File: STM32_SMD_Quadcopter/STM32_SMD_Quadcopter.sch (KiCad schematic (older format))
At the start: 70 parts, among them J1 PWR, J2 USB_B_Micro, J3 Micro_SD_Card_Det, J4 DEBUG, J5 DSMX, M1 Brushed_DC, M2 Brushed_DC, M3 Brushed_DC, M4 Brushed_DC, Q1 IRLML6244TR, Q2 IRLML6244TR, Q3 IRLML6244TR, Q4 IRLML6244TR, Q5 2N7002, SW1 SW_Push, U1 AMS1117-3.3, U2 AMS1117-1.8, U3 FT230XQ, U4 STM32F446RETx, U5 ICM-20948, Y1 16MHz X322516MLB4SI

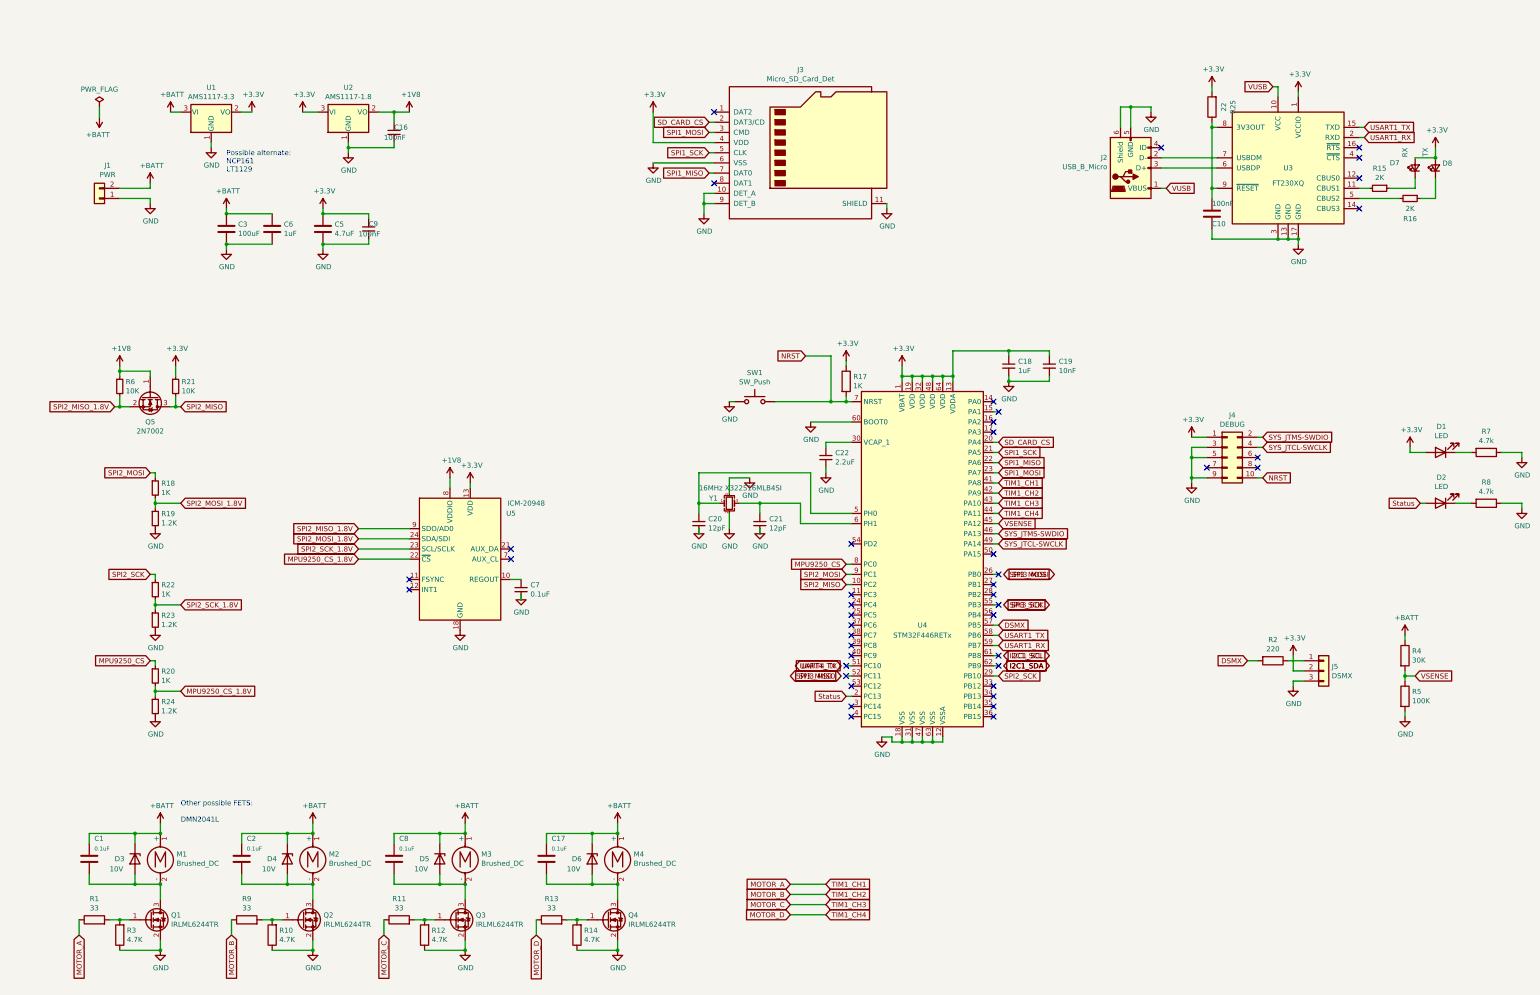
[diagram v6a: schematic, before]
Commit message: completed switchover to MPU6050
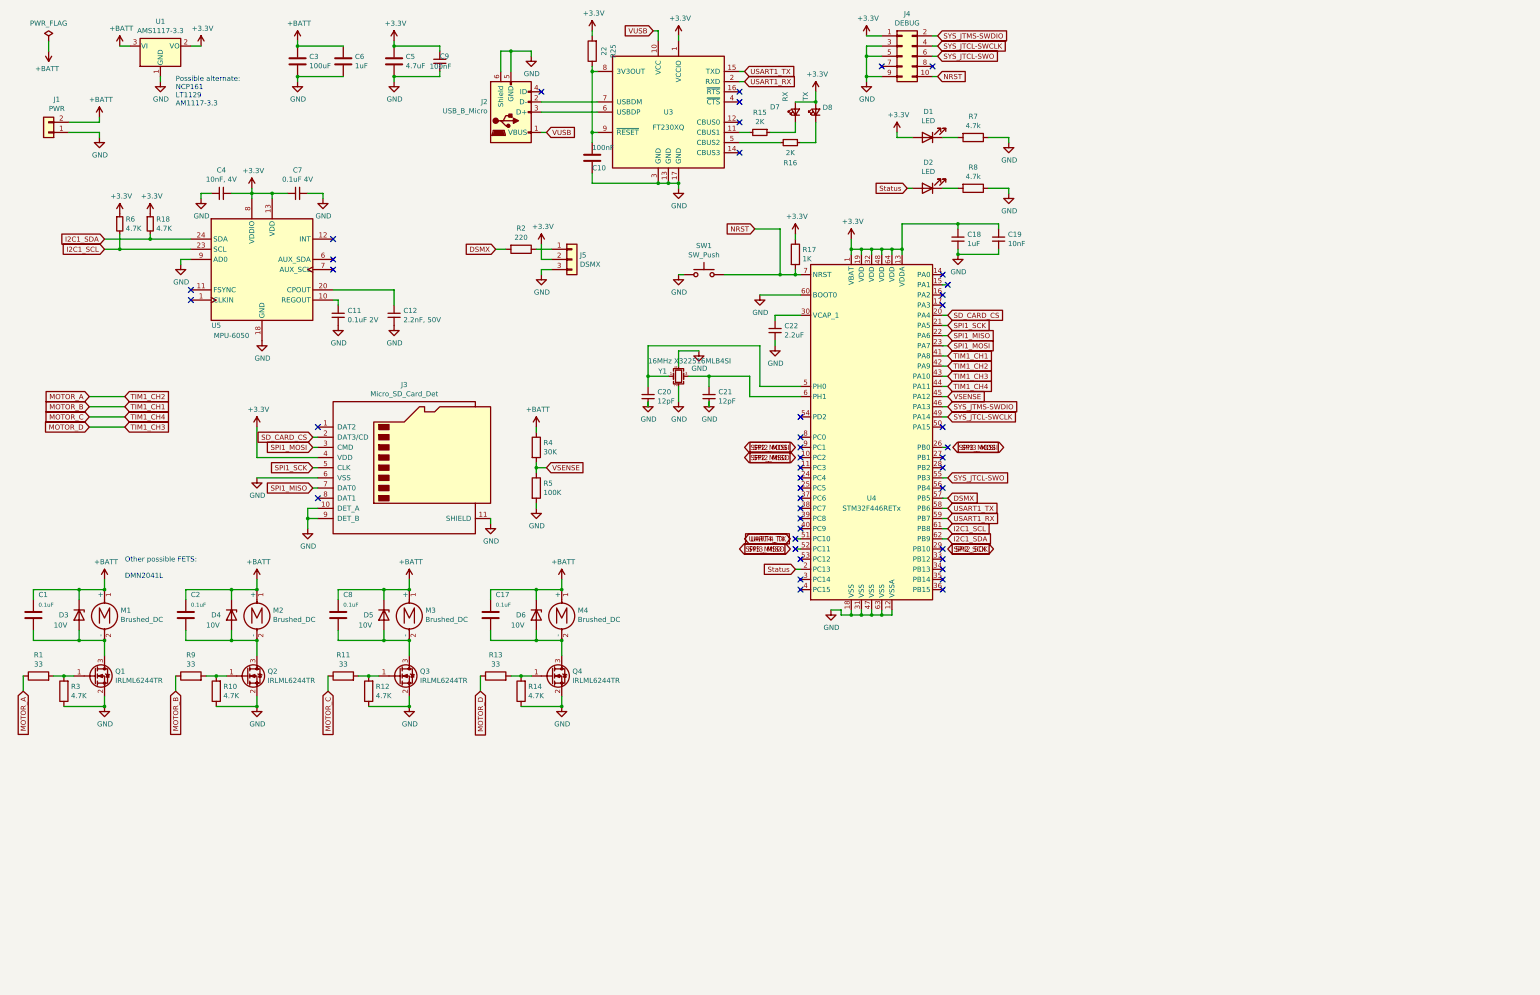
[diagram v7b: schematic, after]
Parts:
- removed C16: 100nF, Capacitor_SMD:C_0402_1005Metric, symbol Device:C_Small
- removed Q5: 2N7002, Package_TO_SOT_SMD:SOT-23, symbol Transistor_FET:2N7002
- removed R19, R23, R24: 1.2K, Resistor_SMD:R_0402_1005Metric, symbol Device:R_Small
- removed R20, R22: 1K, Resistor_SMD:R_0402_1005Metric, symbol Device:R_Small
- removed R21: 10K, Resistor_SMD:R_0402_1005Metric, symbol Device:R_Small
- removed U2: AMS1117-1.8, Package_TO_SOT_SMD:SOT-223-3_TabPin2, symbol Regulator_Linear:AMS1117-1.8
- removed U5: ICM-20948, Sensor_Motion:InvenSense_QFN-24_3x3mm_P0.4mm, symbol Sensor_Motion:ICM-20948
- added C11: 0.1uF 2V, Capacitor_SMD:C_0402_1005Metric, symbol Device:C_Small
- added C12: 2.2nF, 50V, Capacitor_SMD:C_0805_2012Metric, symbol Device:C_Small
- added C4: 10nF, 4V, Capacitor_SMD:C_0402_1005Metric, symbol Device:C_Small
- added U5: MPU-6050, Sensor_Motion:InvenSense_QFN-24_4x4mm_P0.5mm, symbol Sensor_Motion:MPU-6050
- C7: value 0.1uF -> 0.1uF 4V
- R18: value 1K -> 4.7K; footprint Resistor_SMD:R_0402_1005Metric -> Resistor_SMD:R_0603_1608Metric
- R6: value 10K -> 4.7K; footprint Resistor_SMD:R_0402_1005Metric -> Resistor_SMD:R_0603_1608Metric
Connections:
- net +1V8 is gone; now on net +3V3: R6.1
- net SPI2_MISO_1.8V is gone; now on net I2C1_SCL: R6.2
- net SPI2_MOSI_1.8V is gone; now on net I2C1_SDA: R18.2
- net +3V3: now also C7.1, R18.1, C4.2, U5.13 (VDD), U5.8 (VDDIO)
- net GND: now also C11.2, C12.2, C4.1, U5.18 (GND), U5.9 (AD0)
- net I2C1_SCL: now also U4.61 (PB8), U5.23 (SCL)
- net I2C1_SDA: now also U4.62 (PB9), U5.24 (SDA)
- net MOTOR_A: now also U4.42 (PA9); no longer U4.41 (PA8)
- net MOTOR_B: now also U4.41 (PA8); no longer U4.42 (PA9)
- net MOTOR_C: now also U4.44 (PA11); no longer U4.43 (PA10)
- net MOTOR_D: now also U4.43 (PA10); no longer U4.44 (PA11)
- net SPI2_MISO: no longer U4.10 (PC2)
- net SPI2_MOSI: no longer R18.1, U4.9 (PC1)
- net SPI2_SCK: no longer U4.29 (PB10)
- net SYS_JTCL-SWO: now reaches U4.55 (PB3)
- net SYS_JTCL-SWO: now also J4.6 (Pin_6)
- net MPU9250_CS: no longer names the net of U4.8 (PC0)
- new net: C11.1, U5.10 (REGOUT)
- new net: C12.1, U5.20 (CPOUT)
- no-connect marks 43 -> 44
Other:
- note added: "Possible alternate: \nNCP161\nLT1129\nAM1117-3.3\n"
- note removed: "Possible alternate: \nNCP161\nLT1129"
- moved on the sheet: C1, C10, C17, C18, C19, C2, C20, C21, C22, C3, C5, C6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

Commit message: Finished and almost ready for purchase, with stm32f446RET6 and FT230XQ
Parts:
- C1, C10, C11, C17, C2, C7, C8, C9: LCSC (none) -> C1525; LCSC Part # (none) -> C1525
- C12: LCSC (none) -> C28260; LCSC Part # (none) -> C28260
- C18, C6: LCSC (none) -> C15849; LCSC Part # (none) -> C15849
- C19: LCSC (none) -> C57112; LCSC Part # (none) -> C57112
- C20, C21: LCSC (none) -> C38523; LCSC Part # (none) -> C38523
- C22: LCSC (none) -> C23630; LCSC Part # (none) -> C23630
- C3, C5, D3, D4, D5, D6, J1, J2, J3, J4, J5, M1, M2, M3, M4, Q1, Q2, Q3, Q4, SW1, U1: JLCPCB BOM (none) -> 0
- C4: LCSC (none) -> C15195; LCSC Part # (none) -> C15195
- D1: LCSC (none) -> C72038; LCSC Part # (none) -> C72038
- D2: LCSC (none) -> C72043; LCSC Part # (none) -> C72043
- D7: LCSC (none) -> C72041; LCSC Part # (none) -> C72041
- D8: LCSC (none) -> C2286; LCSC Part # (none) -> C2286
- R1, R11, R13, R9: LCSC (none) -> C23140; LCSC Part # (none) -> C23140
- R10, R12, R14, R18, R3, R6, R7, R8: LCSC (none) -> C23162; LCSC Part # (none) -> C23162
- R15, R16: LCSC (none) -> C22975; LCSC Part # (none) -> C22975
- R17: LCSC (none) -> C21190; LCSC Part # (none) -> C21190
- R2: LCSC (none) -> C22962; LCSC Part # (none) -> C22962
- R25: LCSC (none) -> C25092; LCSC Part # (none) -> C25092
- R4: LCSC (none) -> C22984; LCSC Part # (none) -> C22984
- R5: LCSC (none) -> C25803; LCSC Part # (none) -> C25803
- U3: LCSC (none) -> C128629; LCSC Part # (none) -> C128629
- U4: LCSC (none) -> C69336; LCSC Part # (none) -> C69336
- U5: LCSC (none) -> C24112; LCSC Part # (none) -> C24112
- Y1: LCSC (none) -> C13738; LCSC Part # (none) -> C13738
